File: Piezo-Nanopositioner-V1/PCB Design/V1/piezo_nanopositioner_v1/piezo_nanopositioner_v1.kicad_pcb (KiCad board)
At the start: 2 copper layers, 99 parts, among them J101 Conn_01x03_Pin, J2 RF2-04A-T-00-50-G, J201 Conn_01x10_Pin, J202 RF2-04A-T-00-50-G, J301 Conn_01x10_Pin, J302 RF2-04A-T-00-50-G, J401 Conn_01x10_Pin, J402 RF2-04A-T-00-50-G, U1 TDA2050, U2 DAC0800LCM, U201 TL431AIDBZR, U202 DAC0800LCM, U203 TDA2050, U3 TL431AIDBZR, U301 TL431AIDBZR, U302 DAC0800LCM, U303 TDA2050, U4 TL431AIDBZR, U401 TL431AIDBZR, U402 DAC0800LCM, U403 TDA2050

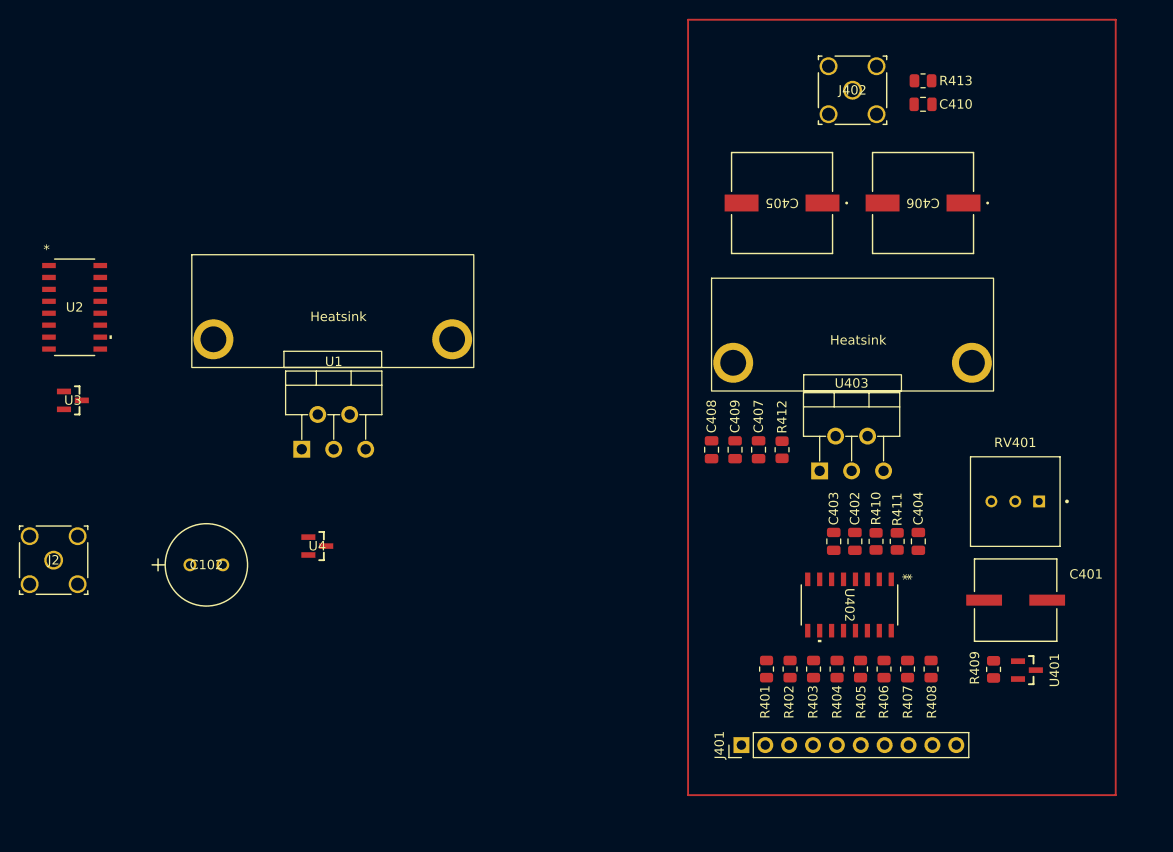
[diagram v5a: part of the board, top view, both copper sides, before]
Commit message: finished routing the traces, added teardrops to traces.
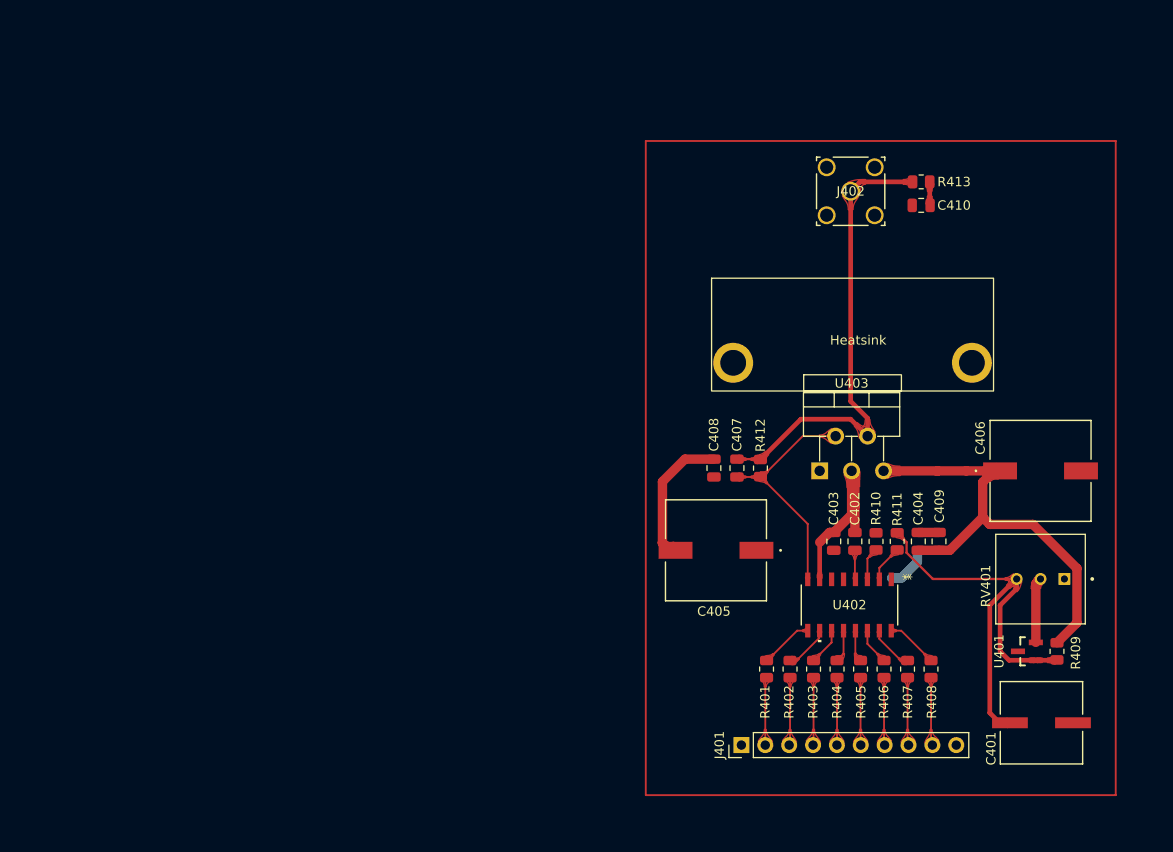
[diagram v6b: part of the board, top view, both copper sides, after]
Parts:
- removed C102: 100uF 50V, Capacitor_THT:CAP_YX_8X11P5_RUB
- removed the Heatsink at (58.2, 74.5)
- removed J2: RF2-04A-T-00-50-G, RF:CONN_RF2-04A-T-00-50-G_ADM
- removed U1: TDA2050, Package_TO_SOT_THT:TO-220-5_P3.4x3.7mm_StaggerOdd_Lead3.8mm_Vertical
- removed U2: DAC0800LCM, DAC0800LCM_SMT:M16A_TEX
- removed U3, U4: TL431AIDBZR, TL431AIDBZR:DBZ0003A_N
- moved C405 37.6 mm to (99.0, 97.0)
- moved C406 31.1 mm to (133.5, 88.5), turned to 0 degrees
- moved C409 23.8 mm to (122.7, 96.0), turned to 90 degrees
- moved C401 13.3 mm to (133.6, 115.3)
- moved C410 10.8 mm to (120.8, 60.2)
- moved J402 10.8 mm to (113.3, 58.8)
- moved R413 10.8 mm to (120.8, 57.8)
- moved RV401 8.68 mm to (133.5, 100.0)
- moved R409 7.02 mm to (135.3, 107.7), turned to -90 degrees
- moved C407 3.02 mm to (101.2, 88.2)
- moved R412 3.02 mm to (103.7, 88.2)
- moved U401 2.00 mm to (132.1, 107.7), turned to 180 degrees
- moved C408 1.97 mm to (98.8, 88.2)
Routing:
- net +15V: track 0.00 -> 52.6 mm
- net Net-(J402-Sig): track 0.00 -> 50.3 mm
- net /Z_DAC/VRef+: track 0.00 -> 48.3 mm
- net -15V: track 0.00 -> 34.6 mm
- net Net-(U402-IOUT): track 0.00 -> 25.4 mm
- net Net-(J401-Pin_9): track 0.00 -> 7.24 mm
- net Net-(J401-Pin_2): track 0.00 -> 7.23 mm
- net Net-(J401-Pin_8): track 0.00 -> 7.22 mm
- net Net-(J401-Pin_3): track 0.00 -> 7.21 mm
- net Net-(J401-Pin_7): track 0.00 -> 7.20 mm
- net Net-(J401-Pin_4): track 0.00 -> 7.20 mm
- net Net-(J401-Pin_6): track 0.00 -> 7.19 mm
- net Net-(J401-Pin_5): track 0.00 -> 7.18 mm
- net Net-(U401-REF): track 0.00 -> 6.96 mm
- net Net-(U402-B1): track 0.00 -> 5.70 mm
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
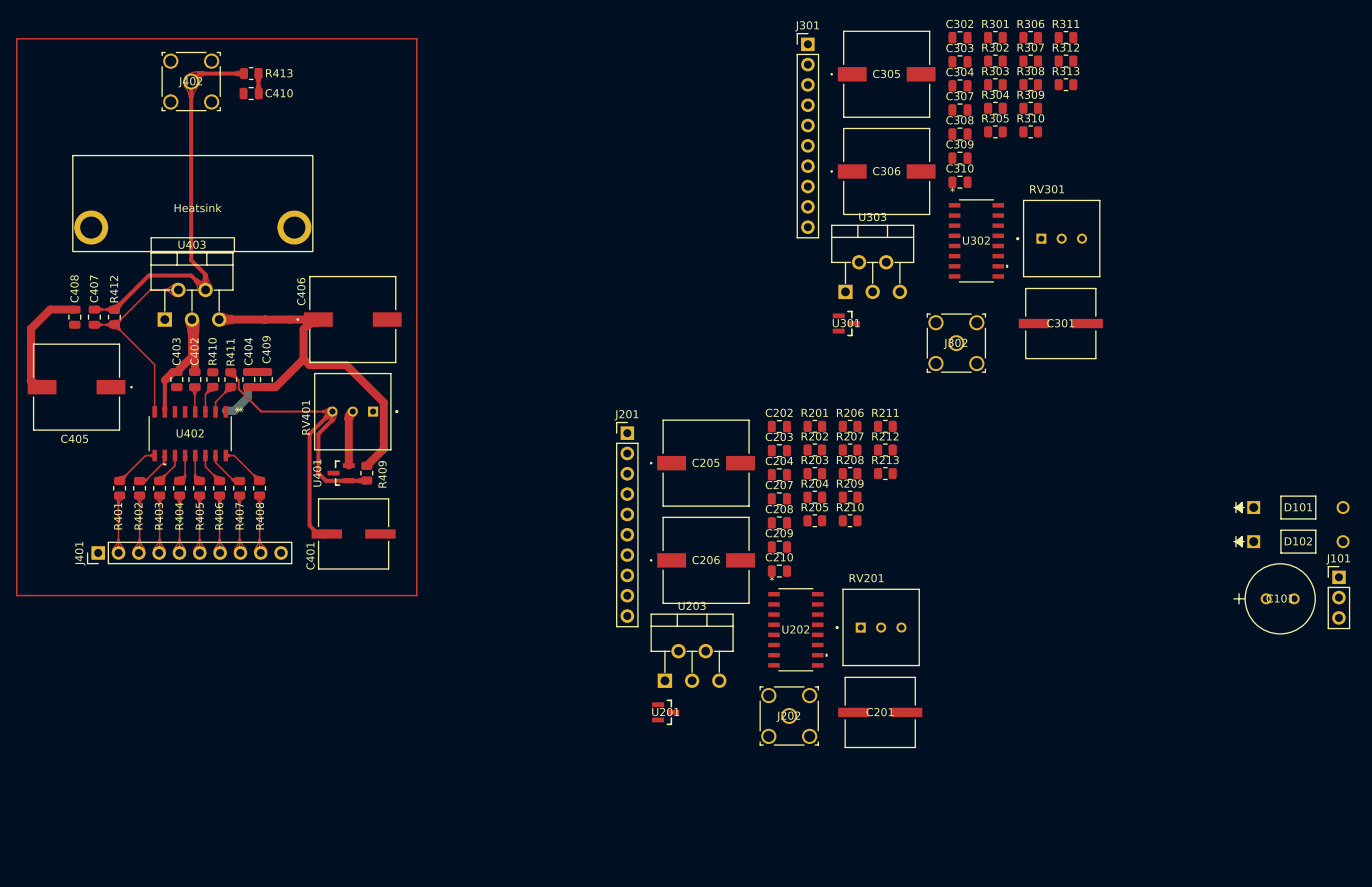
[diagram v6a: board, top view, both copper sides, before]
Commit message: started placing vias, created +/-15V zones. Created ground plane on second layer.
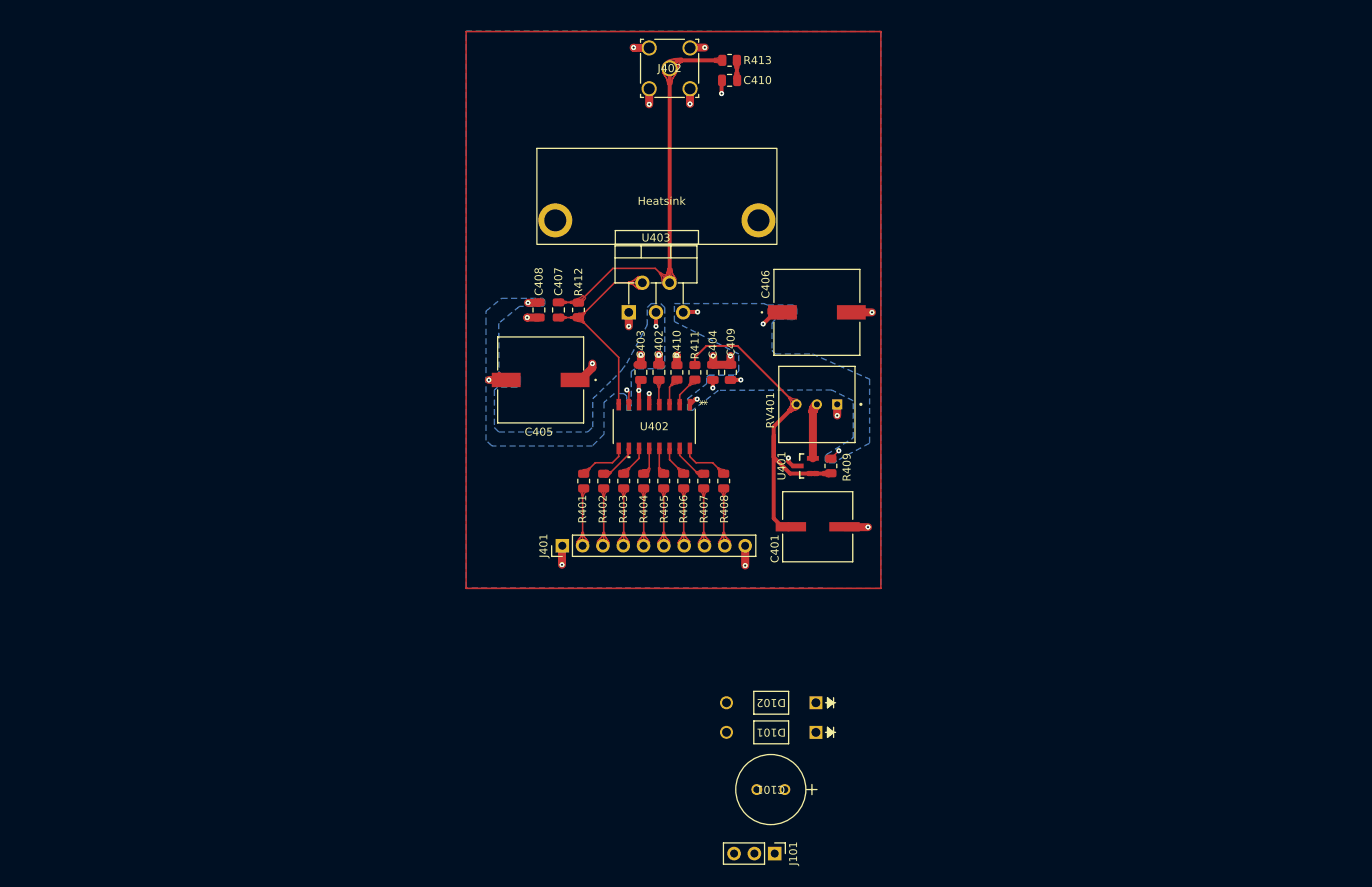
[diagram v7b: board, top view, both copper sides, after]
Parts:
- removed C201, C301: 47u, Capacitor_SMD:CAP_EEFC_E_PAN
- removed C202, C302: 10n, Capacitor_SMD:C_0805_2012Metric
- removed C203, C204, C208, C209, C303, C304, C308, C309: 100n, Capacitor_SMD:C_0805_2012Metric
- removed C205, C206, C305, C306: 470u, Capacitor_THT:CAP_ZSU_G12_PAN
- removed C207, C307: 68p, Capacitor_SMD:C_0805_2012Metric
- removed C210, C310: 4.7n, Capacitor_SMD:C_0805_2012Metric
- removed J201, J301: Conn_01x10_Pin, Connector_PinHeader_2.54mm:PinHeader_1x10_P2.54mm_Vertical
- removed J202, J302: RF2-04A-T-00-50-G, RF:CONN_RF2-04A-T-00-50-G_ADM
- removed R201, R202, R203, R204, R205, R206, R207, R208, R301, R302, R303, R304, R305, R306, R307, R308: 100R, Resistor_SMD:R_0805_2012Metric
- removed R209, R309: 1k, Resistor_SMD:R_0805_2012Metric
- removed R210, R211, R310, R311: 5k, Resistor_SMD:R_0805_2012Metric
- removed R212, R312: 15k, Resistor_SMD:R_0805_2012Metric
- removed R213, R313: 10R, Resistor_SMD:R_0805_2012Metric
- removed RV201, RV301: 10k, Potentiometer_THT:TRIM_COM-09806
- removed U201, U301: TL431AIDBZR, TL431AIDBZR:DBZ0003A_N
- removed U202, U302: DAC0800LCM, DAC0800LCM_SMT:M16A_TEX
- removed U203, U303: TDA2050, Package_TO_SOT_THT:TO-220-5_P3.4x3.7mm_StaggerOdd_Lead3.8mm_Vertical
- moved J101 78.5 mm to (186.2, 155.2), turned to -90 degrees
- moved C101 64.7 mm to (187.5, 147.2), turned to 180 degrees
- moved D101 61.5 mm to (191.4, 140.1), turned to 180 degrees
- moved C410 59.8 mm to (180.6, 58.6)
- moved J402 59.8 mm to (173.1, 57.1)
- moved R413 59.8 mm to (180.6, 56.1)
- moved D102 58.3 mm to (191.4, 136.4), turned to 180 degrees
- moved C407 58.0 mm to (159.2, 87.3)
- moved C409 58.0 mm to (180.7, 95.1)
- moved J401 58.0 mm to (159.7, 116.8)
- moved R412 58.0 mm to (161.7, 87.3)
- moved U402 58.0 mm to (171.2, 101.9)
- moved C401 58.0 mm to (191.6, 114.4)
- moved C402 58.0 mm to (171.8, 95.1)
- moved C403 58.0 mm to (169.5, 95.1)
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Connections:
- J402 pad 2: (no net) -> GND
- J402 pad 3: (no net) -> GND
- J402 pad 4: (no net) -> GND
- J402 pad 5: (no net) -> GND
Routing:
- net +15V: track 52.6 -> 10.4 mm, vias 0 -> 6
- net GND: track 2.20 -> 40.7 mm, vias 0 -> 19
- net -15V: track 34.6 -> 10.9 mm, vias 0 -> 6
- net /Z_DAC/VRef+: track 48.3 -> 46.0 mm
- net Net-(U402-B8): track 5.55 -> 6.15 mm
- net Net-(U402-B1): track 5.70 -> 6.29 mm
- added copper zone on B.Cu, net +15V
- added copper zone on B.Cu, net -15V
- added copper zone on B.Cu, net GND
